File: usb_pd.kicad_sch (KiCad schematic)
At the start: 24 parts, among them J15 USBC-PD, J16 CONN_2PIN, Q1 SQJ459EP-T2_GE3, U5 STUSB4531QTR

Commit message: Isole la liaison ESP32<->STUSB4531 (ISO1640BD + DPC817), USB-PD rejoint GND_PRI
Le bus de supervision I2C/ALERT (STUSB_SCL/STUSB_SDA/STUSB_ALERT) reliait
directement GPIO22/23/21 aux pins de U1, sans isolation. Isole avec :
- ISO1640BD (TI, 8-SOIC, isolation basique 3000VRMS) pour SCL/SDA -
  symbole dessine a la main (absent des bibliotheques stock), empreinte
  SOIC-8 standard.
- DPC817 (optocoupleur, NRND mais empreinte generique standard 4 broches)
  pour ALERT - brochage repris du symbole stock PC817, empreinte SL-4
  dessinee a la main (aucune empreinte stock ne correspondait).

Reutilise les pull-ups existants R45/R46/R47 (4,7k vers 3V3_ESP32) comme
cote Side 1 de l'isolateur, simplement renommes (ESP32_SCL_ISO/
ESP32_SDA_ISO/ESP32_ALERT_ISO). VREG_2V7 (deja existant) alimente le
Side 2, avec 2 pull-ups neufs (2,2k) + 1 resistance limiteuse LED (330R).

Clarification plus large de l'utilisateur : tout usb_pd.kicad_sch (16
occurrences de GND, pas seulement l'isolateur) rejoint GND_PRI - le
sous-systeme USB-PD (20V) appartient au meme domaine primaire que le
connecteur 11-25V, separe de GND par les convertisseurs 3,3V existants.
GND_PRI etait deja classe Isole_Primaire dans shield.kicad_pro, aucune
nouvelle regle necessaire.

Caracterise les deux composants dans composants-datasheets/ (nouvelle
famille isolator_digital, lint propre).

Bug trouve en implementant : (shape power_in) est un mot-cle invalide
pour global_label, fait echouer la connexion ERC silencieusement -
documente en decision #27 pour ne pas le reproduire.

Verifie : ERC feuille par feuille/categorie contre l'etat precedent,
aucune regression (le seul power_pin_not_driven neuf sur GND_PRI/U5 est
attendu, meme caracteristique deja acceptee que VIN_PWR/GND_PRI sur DC).

Co-Authored-By: Claude Sonnet 5 <noreply@anthropic.com>
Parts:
- added R55, R56: 2.2k, Resistor_SMD:R_0805_2012Metric, symbol Device:R
- added R57: 330R, Resistor_SMD:R_0805_2012Metric, symbol Device:R
- added U6: ISO1640BD, Package_SO:SOIC-8_3.9x4.9mm_P1.27mm, symbol Power_Parts:ISO1640BD
- added U7: DPC817, lib:DPC817, symbol Power_Parts:DPC817
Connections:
- net 3V3_ESP32: now also U6.1 (VCC1)
- net GND: now also U6.4 (GND1), U7.3 (E); no longer C62.2, C63.2, C64.2, C65.2, D40.2 (A), D41.2 (A), D43.3 (A), J15.A12 (GND), J15.B12 (GND), J15.MH1, J15.MH2, J15.MH3, J15.MH4, J16.2, R39.2, U5.12 (GND)
- net STUSB_ALERT: now also U7.2 (K); no longer R47.1
- net STUSB_SCL: now also R55.2, U6.6 (SCL2); no longer R45.1
- net STUSB_SDA: now also R56.2, U6.7 (SDA2); no longer R46.1
- net VREG_2V7: now also R55.1, R56.1, R57.1, U6.8 (VCC2)
- new net: R57.2, U7.1 (A)
- new net ESP32_ALERT_ISO: R47.1, U7.4 (C)
- new net ESP32_SCL_ISO: R45.1, U6.3 (SCL1)
- new net ESP32_SDA_ISO: R46.1, U6.2 (SDA1)
- new net GND_PRI: C62.2, C63.2, C64.2, C65.2, D40.2 (A), D41.2 (A), D43.3 (A), J15.A12 (GND), J15.B12 (GND), J15.MH1, J15.MH2, J15.MH3, J15.MH4, J16.2, R39.2, U5.12 (GND), U6.5 (GND2)

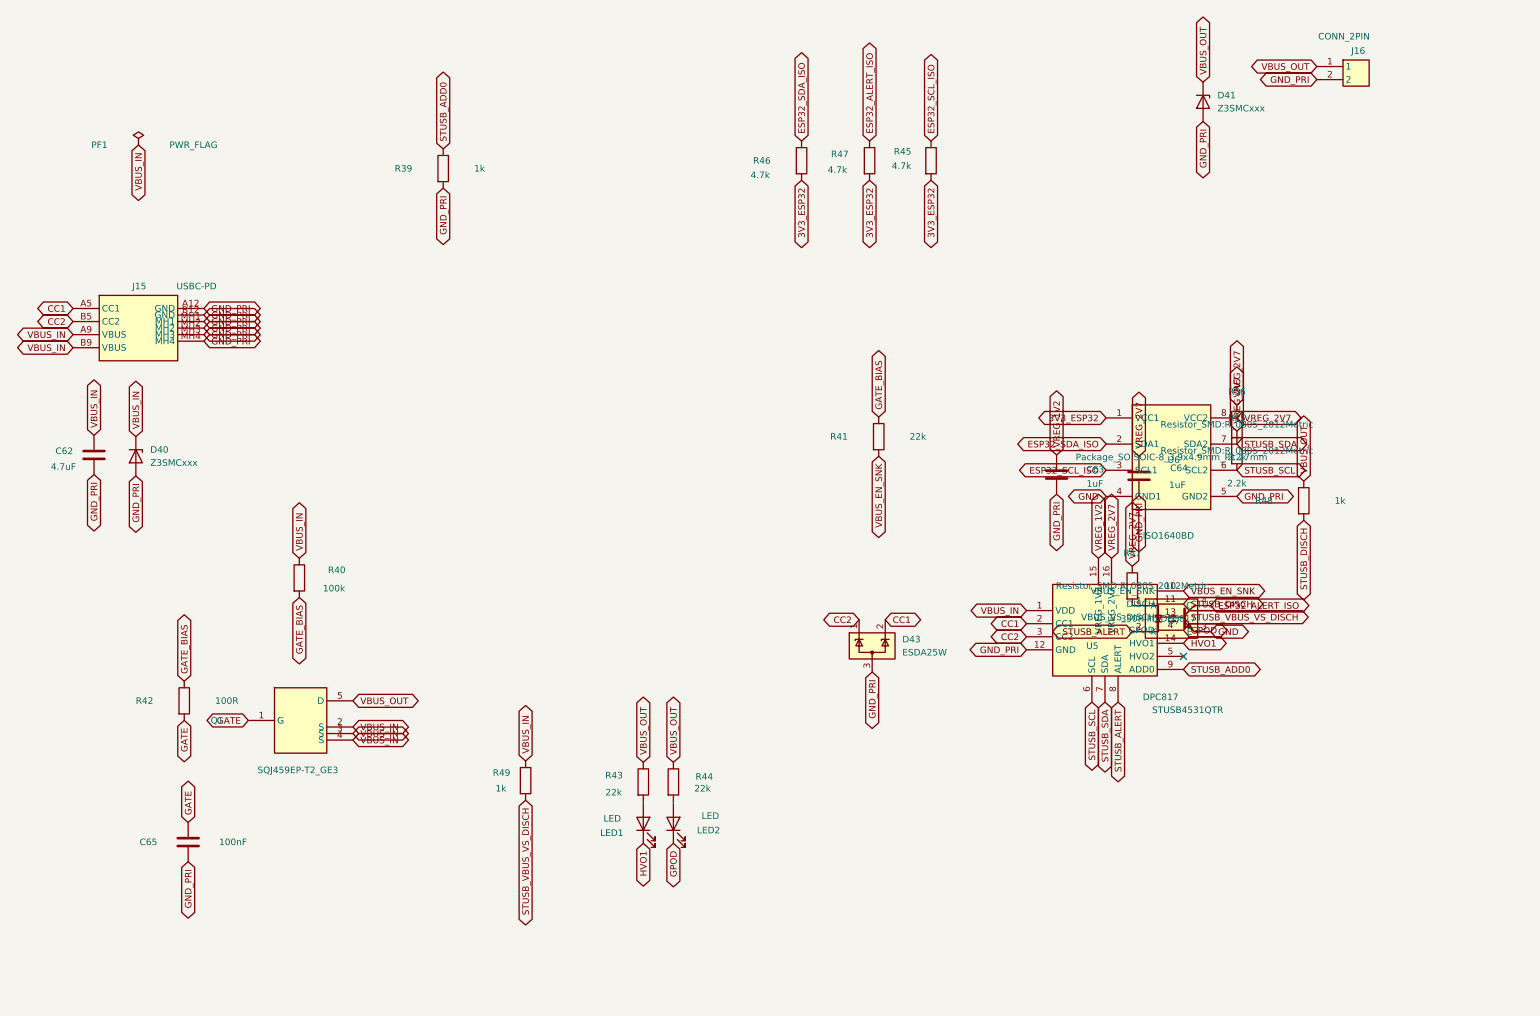
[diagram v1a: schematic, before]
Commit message: Respace les composants d'isolation sur usb_pd.kicad_sch (anti-chevauchement)
ISO1640BD/DPC817/R55/R56/R57 etaient positionnes par coincidence de pin
uniquement (connexions par coordonnee), sans tenir compte du corps des
composants : certains se touchaient (ecart nul), aucun n'avait les 15mm
demandes. Deplaces dans une zone vide de la feuille (sous le contenu
existant), connexions refaites entierement par global_label nomme (plus
de contrainte de coincidence physique) - verifie programmatiquement que
les 10 paires de composants neufs ont toutes >= 15mm d'ecart entre corps.

ERC identique a avant (meme diff attendu), rien de casse par le deplacement.

Co-Authored-By: Claude Sonnet 5 <noreply@anthropic.com>
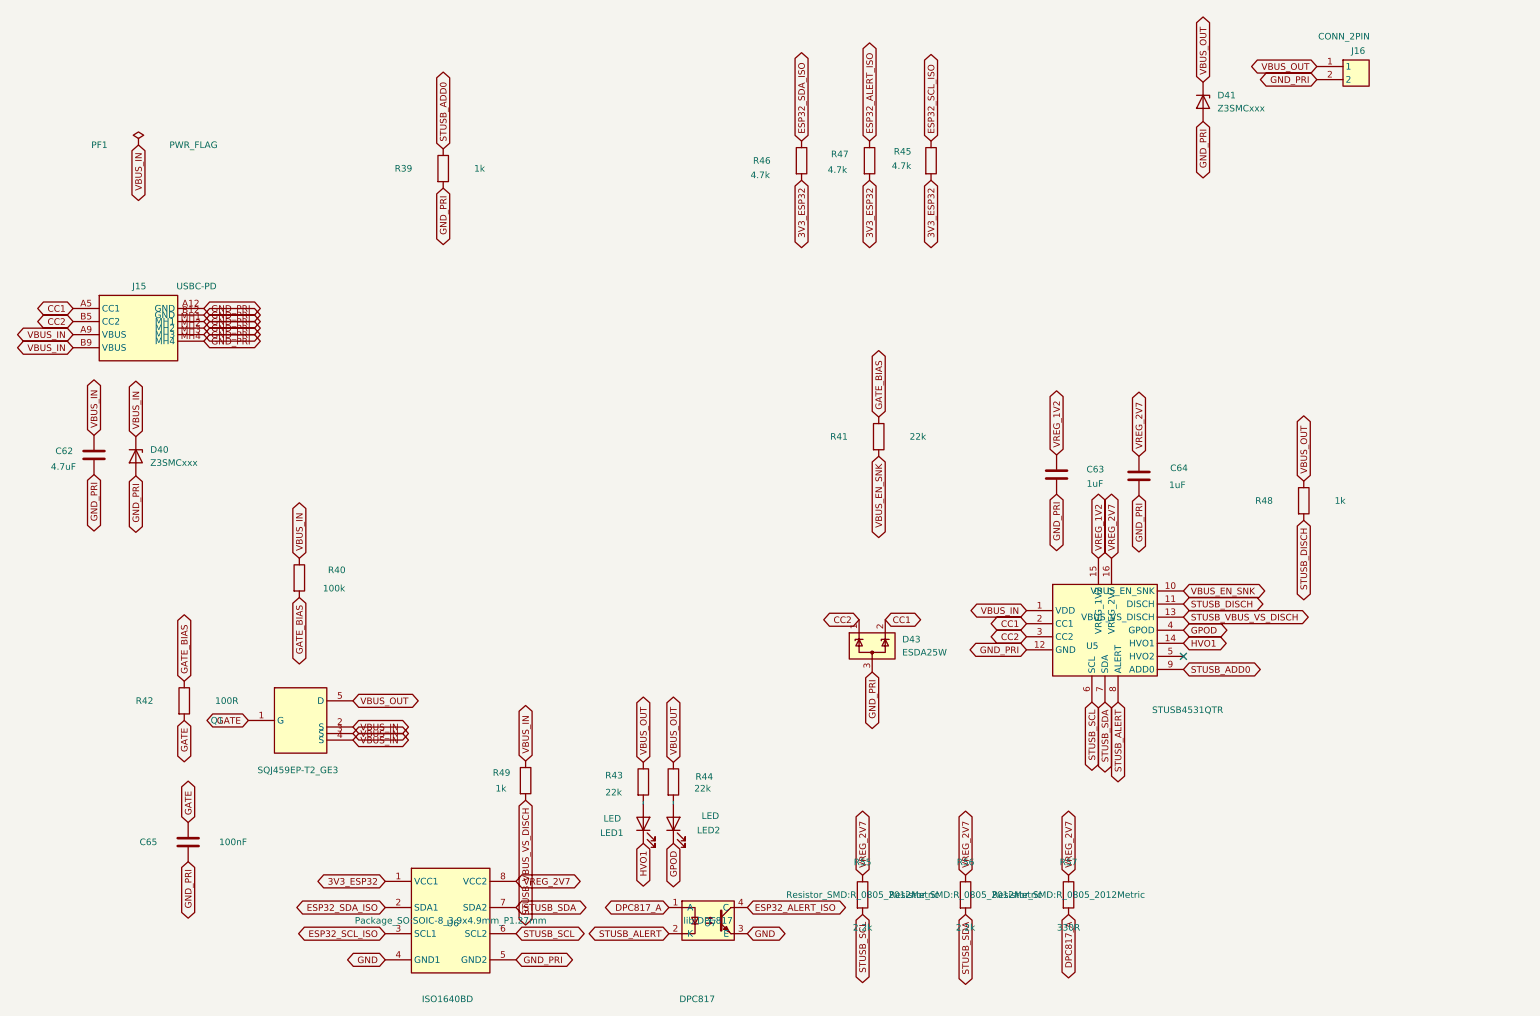
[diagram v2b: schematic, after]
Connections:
- net DPC817_A: now reaches R57.2, U7.1 (A)

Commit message: Remplace DPC817 (NRND, empreinte maison) par TCMT1100 (Vishay, standard)
U7 passe d'un optocoupleur Diodes Inc. en boitier SL-4 fait main a un
TCMT1100 Vishay dont le symbole ET l'empreinte (SOP-4_4.4x2.6mm_P1.27mm)
sont stock KiCad - brochage identique, aucun rewiring necessaire.
Footprint PCB reconstruit a la main via kipy (pads, silkscreen,
courtyard, contour fab, identite de librairie). Route et groupe aussi
les 5 nouveaux trios de protection ADC (D44-48/R50-54/C66-70) en
copiant le gabarit des trios existants, et uniformise a 0,5mm toutes
les pistes internes des 43 groupes PROT_*.

Decision #28 dans doc/decisions.md.

Co-Authored-By: Claude Sonnet 5 <noreply@anthropic.com>
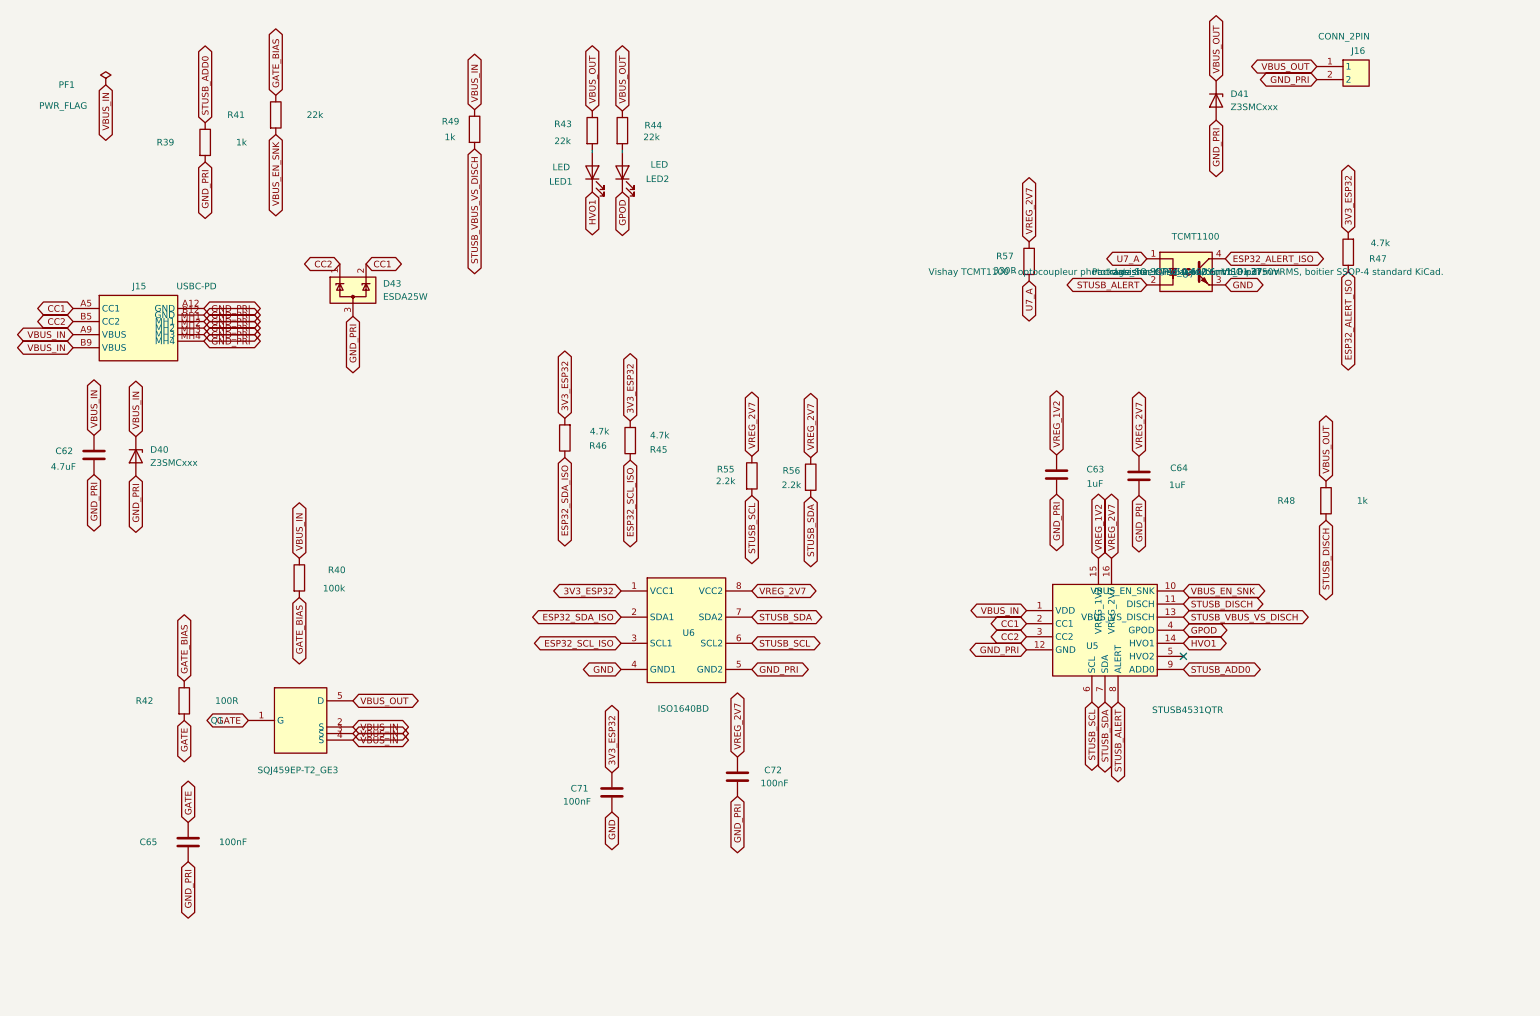
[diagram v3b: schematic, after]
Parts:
- added C71, C72: 100nF, Capacitor_SMD:C_0805_2012Metric, symbol Device:C
- U7: value DPC817 -> TCMT1100; footprint lib:DPC817 -> Package_SO:SOP-4_4.4x2.6mm_P1.27mm; symbol Power_Parts:DPC817 -> Isolator:TCMT1100
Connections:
- net 3V3_ESP32: now also C71.1
- net GND: now also C71.2
- net GND_PRI: now also C72.2
- net VREG_2V7: now also C72.1
- net DPC817_A renamed U7_A
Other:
- moved on the sheet: D41, D43, LED1, LED2, R39, R41, R43, R44, R45, R46, R47, R48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
